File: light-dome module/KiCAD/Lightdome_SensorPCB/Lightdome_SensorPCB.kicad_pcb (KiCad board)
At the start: 2 copper layers, 17.8 x 25.4 mm, 6 parts, among them J1 Conn_01x04, U1 VEML6070, U2 VEML7700-TT, U3 P82B715D

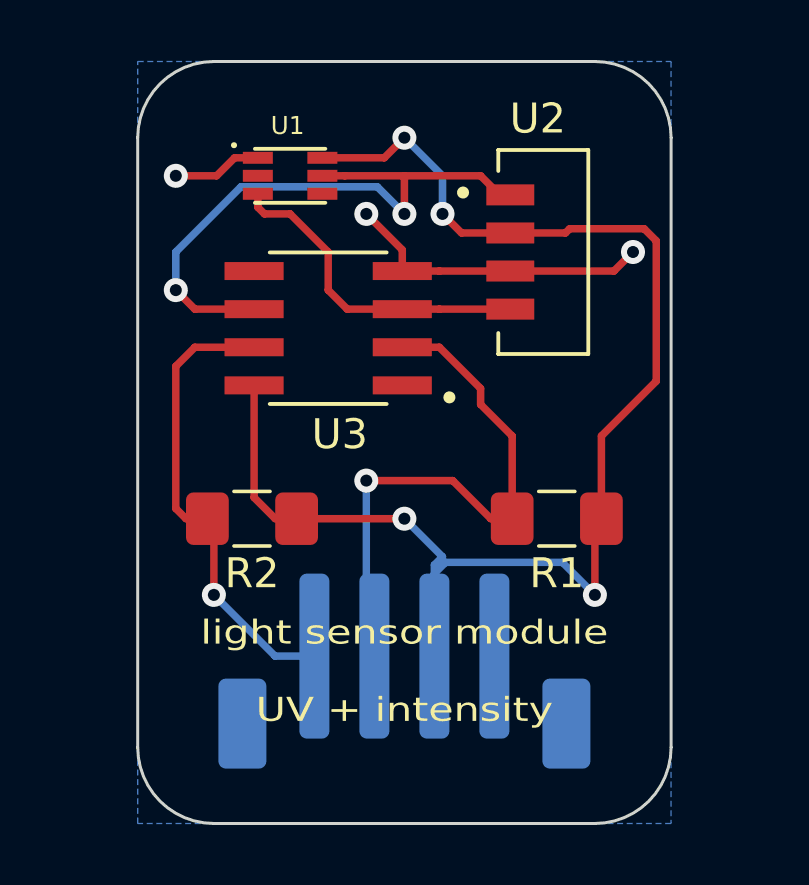
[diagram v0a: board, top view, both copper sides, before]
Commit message: changes in light module PCB
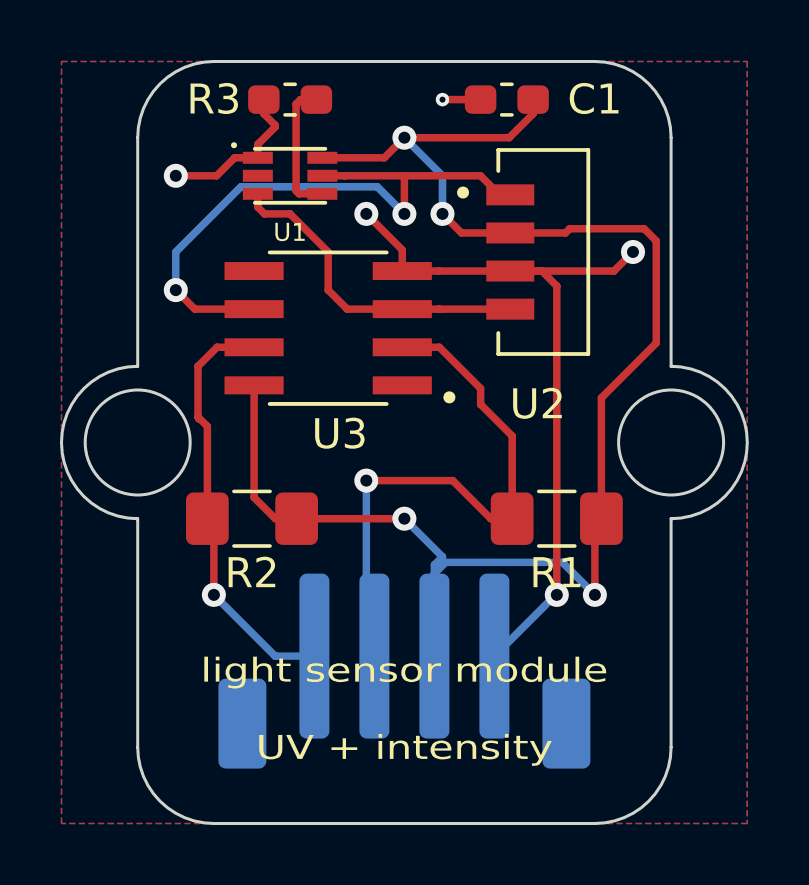
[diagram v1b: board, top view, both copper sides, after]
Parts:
- added C1: 100n, Capacitor_SMD:C_0603_1608Metric_Pad1.05x0.95mm_HandSolder, F.Cu at (146.9, 74.9)
- added R3: 270K, Resistor_SMD:R_0603_1608Metric_Pad1.05x0.95mm_HandSolder, F.Cu at (139.7, 74.9)
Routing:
- net GND: track 13.3 -> 31.9 mm, vias 3 -> 5
- net +3V3: track 49.3 -> 54.4 mm
- net Net-(R3-Pad1): track 0.00 -> 4.54 mm
- net LCL: track 15.6 -> 14.2 mm
- added copper zone on F.Cu, net GND
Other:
- board size 17.8 x 25.4 mm -> 22.9 x 25.4 mm
